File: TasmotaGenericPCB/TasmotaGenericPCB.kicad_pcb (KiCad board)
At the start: 2 copper layers, 27.9 x 24.1 mm, 8 parts, among them J1 Conn_01x04, J2 Conn_01x04, Q1 BUZ11, Q2 BUZ11, U1 ESP-01v090, U2 LD1117S33TR_SOT223

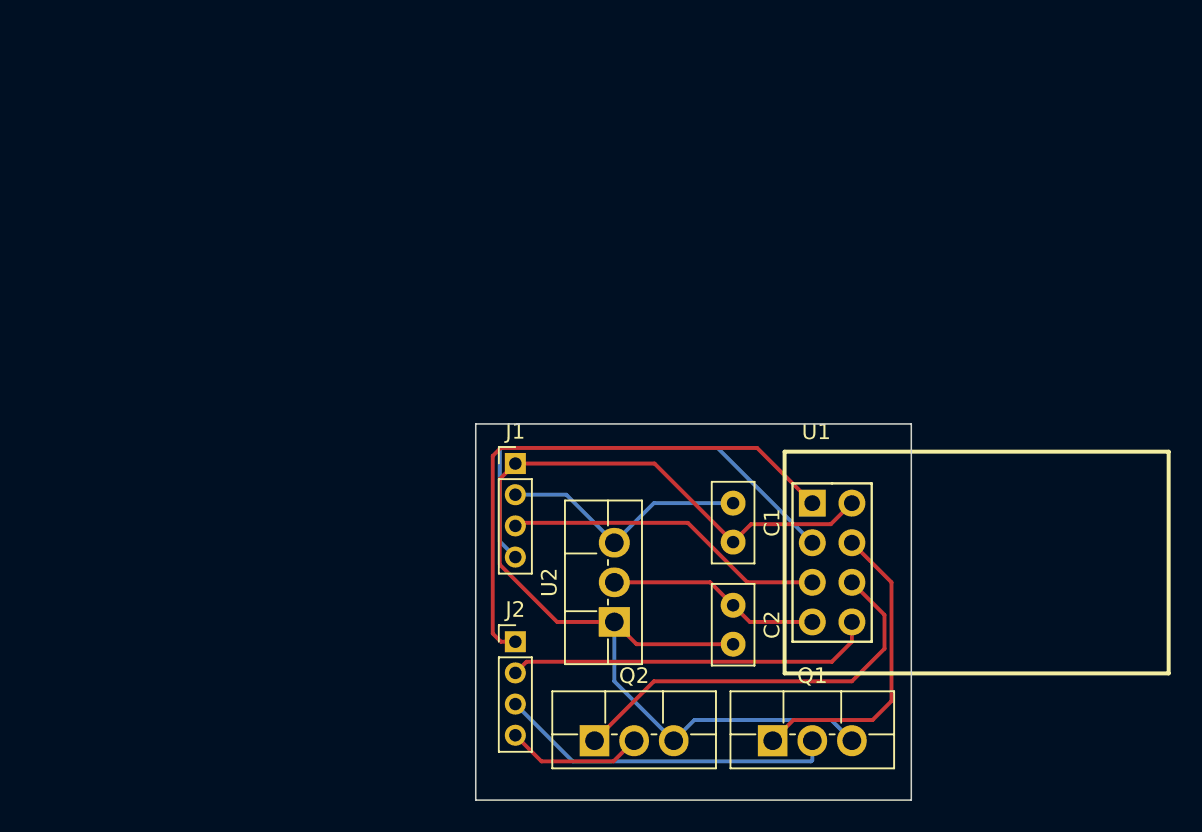
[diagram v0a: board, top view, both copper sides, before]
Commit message: v 2.0 - fixes en pin issues discovered in testing
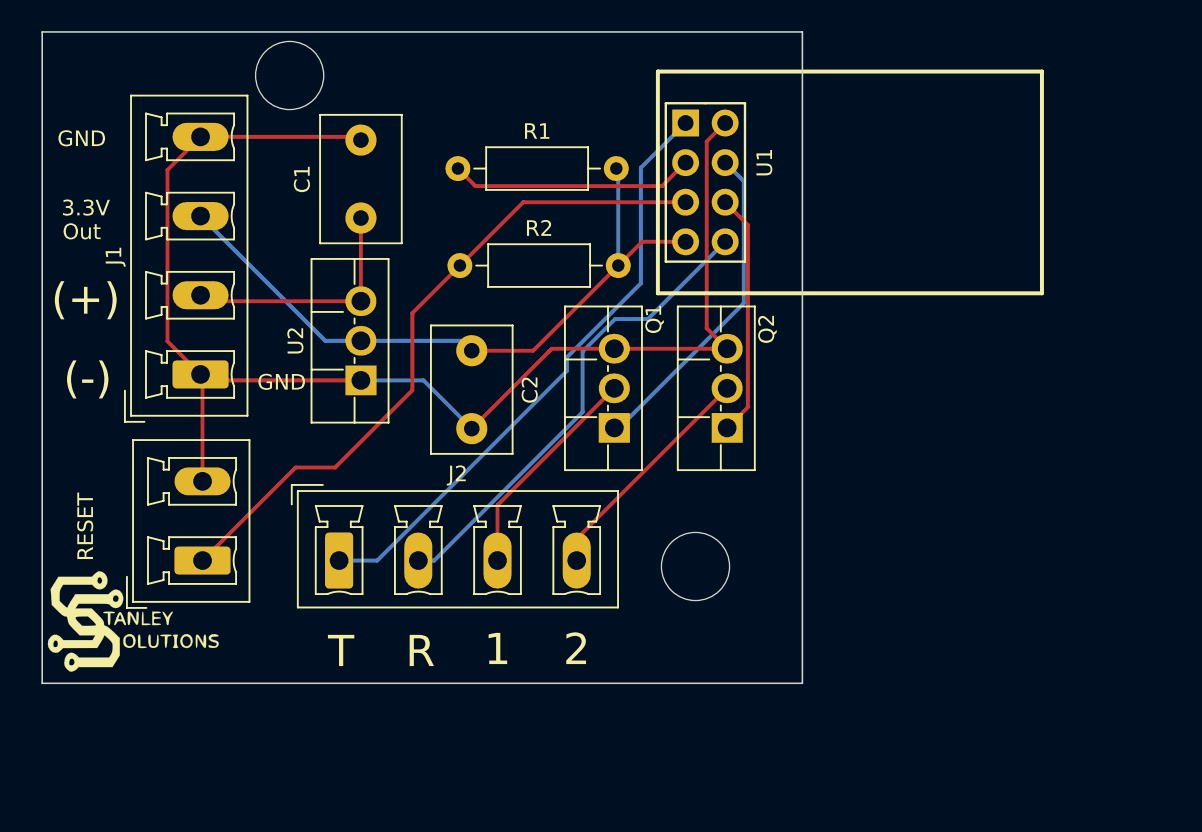
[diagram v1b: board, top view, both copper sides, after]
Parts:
- added G***: LOGO, TasmoTree:StanleySolutionsPCB_m, B.Cu at (122.2, 95.2)
- added G***: LOGO, TasmoTree:StanleySolutionsPCB, F.Cu at (98.2, 120.9)
- added J3: ResetPinout, Connector_Phoenix_MC_HighVoltage:PhoenixContact_MCV_1,5_2-G-5.08_1x02_P5.08mm_Vertical, F.Cu at (103.1, 116.7)
- added R1: 4.7k, Resistors:R_Axial_DIN0207_L6.3mm_D2.5mm_P10.16mm_Horizontal, F.Cu at (119.5, 91.6)
- added R2: 4.7k, Resistors:R_Axial_DIN0207_L6.3mm_D2.5mm_P10.16mm_Horizontal, F.Cu at (119.6, 97.8)
- C1, C2: footprint Capacitors:C_Disc_D5.0mm_W2.5mm_P2.50mm -> Capacitors:C_Disc_D8.0mm_W5.0mm_P5.00mm
- J1, J2: footprint Connectors:PinHeader_1x04_P2.00mm_Vertical -> Connector_Phoenix_MC_HighVoltage:PhoenixContact_MCV_1,5_4-G-5.08_1x04_P5.08mm_Vertical
- moved C1 30.1 mm to (113.3, 94.7), turned to 90 degrees
- moved U1 25.7 mm to (134.1, 88.6)
- moved C2 23.4 mm to (120.4, 103.3)
- moved Q1 22.5 mm to (129.5, 108.2), turned to 90 degrees
- moved U2 22.5 mm to (113.3, 105.2)
- moved Q2 21.8 mm to (136.8, 108.2), turned to 90 degrees
- moved J1 21.0 mm to (103.0, 104.8), turned to 90 degrees
- moved J2 12.4 mm to (111.9, 116.7)
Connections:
- J1 pad 3: Net-(J1-Pad3) -> Net-(C2-Pad1)
- J1 pad 4: Net-(J1-Pad4) -> /GND
- U1 pad 3: Net-(J1-Pad4) -> Net-(R1-Pad1)
- U1 pad 5: Net-(J1-Pad3) -> Net-(J3-Pad1)
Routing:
- net Net-(J3-Pad1): track 0.00 -> 43.4 mm
- net Net-(C2-Pad1): track 13.8 -> 43.9 mm
- net Net-(J1-Pad4): track 29.9 -> 0.00 mm
- net Net-(J1-Pad3): track 20.7 -> 0.00 mm
- net /GND: track 70.4 -> 87.3 mm
- net Net-(R1-Pad1): track 0.00 -> 15.7 mm
- net Net-(Q2-Pad1): track 26.2 -> 15.6 mm
- net Net-(J2-Pad3): track 21.9 -> 14.2 mm
- net Net-(J2-Pad2): track 23.7 -> 30.6 mm
- net Net-(J2-Pad4): track 8.86 -> 15.0 mm
- net Net-(J2-Pad1): track 35.2 -> 38.7 mm
- net Net-(Q1-Pad1): track 19.8 -> 21.1 mm
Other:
- board size 27.9 x 24.1 mm -> 48.8 x 41.8 mm
- board text added: "(+)"
- board text added: "(-)"
- board text added: "1"
- board text added: "2"
- board text added: "3.3V"
- board text added: "GND"
- board text added: "Out"
- board text added: "R"
- board text added: "RESET"
- board text added: "T"
